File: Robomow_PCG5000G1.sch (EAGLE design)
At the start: 22 parts, among them IC1 LM339D, Q401 60N06LC, Q402 N-MOSFETDPACK, T1 2N2222, U400 74AC153D

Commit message: Commit moare reveng
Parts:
- removed IC1: LM339D, linear:LM339D
- removed R2: 2K, rcl:R-EU_R0603
- added C406, C408: (no value), rcl:C-EUC0603
- added JP1: (no value), pinhead:PINHD-2X25
- added Q403: N-MOSFETDPACK, martonmiklos:N-MOSFETDPACK
- added R210, R212, R???: 1K, resistor-dil:4R-NCAT16
- added R4, R422, R423: 2K2, rcl:R-EU_R0603
- added R???1: 2K, rcl:R-EU_R0603
- added TP703: TPB1,27, testpad:TPB1,27
- added U1: LM339M, NSC_By_element14_Batch_1.1:LM339M
- added U401: 74HC14D, 74xx-eu:74HC14D
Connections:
- removed net N$16: C407.2, R3.2
- new net MCU_P14: R210D.2
- new net MCU_P15: R210C.2
- new net MCU_P16: R210B.2
- new net MCU_P26_OUTC16_PIN45: R212B.2
- new net MCU_TA2OUT: R???B.2
- new net MOTOR_HALT?: C410.1, Q402.G, R210B.1, R406.1, R407.1
- new net MOTOR_HALT?1: C406.1, Q403.G, R210C.1
- new net N$15: U400A.1G, U401D.O
- new net N$18: C408.2, R423.1
- new net N$19: JP1.37, JP1.39, JP1.41
- new net N$20: R4.1, U1.-IN3
- new net TO_RJ11_PIN2_FROM_M16C_TXD1: JP1.4
- new net TO_RJ11_PIN_3_FROM_M16C_RXD1: JP1.3
- net GND: now also C406.2, C407.2, Q403.S, R3.2, U1.+IN4, U1.-IN4, U1.GND
- net N$12: now also R???B.1
- net N$14: now also Q403.D, R???1.2; no longer R2.2
- net N$17: now also R210D.1
- net N$5: now also C408.1, R4.2, R422.2, R423.2, U1.OUT3, U401D.I; no longer C410.1, Q402.G, R406.1, R407.1
- net N$6: now also TP703.TP
- net N$7: now also R212B.1
- net N$8: now also R???1.1, U1.+IN3; no longer IC1C.+IN, R2.1
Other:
- note added: "Motor PWM?"
- note added: "Mow PWM"
- note added: "Mow disable"
- note added: "Mow enable"
- note added: "Mow motor running if: 1G low 1C3 high A high B high"
- moved on the sheet: C407, J400, Q400, Q401, R1, R3, R407, R408, R410, R?, T1

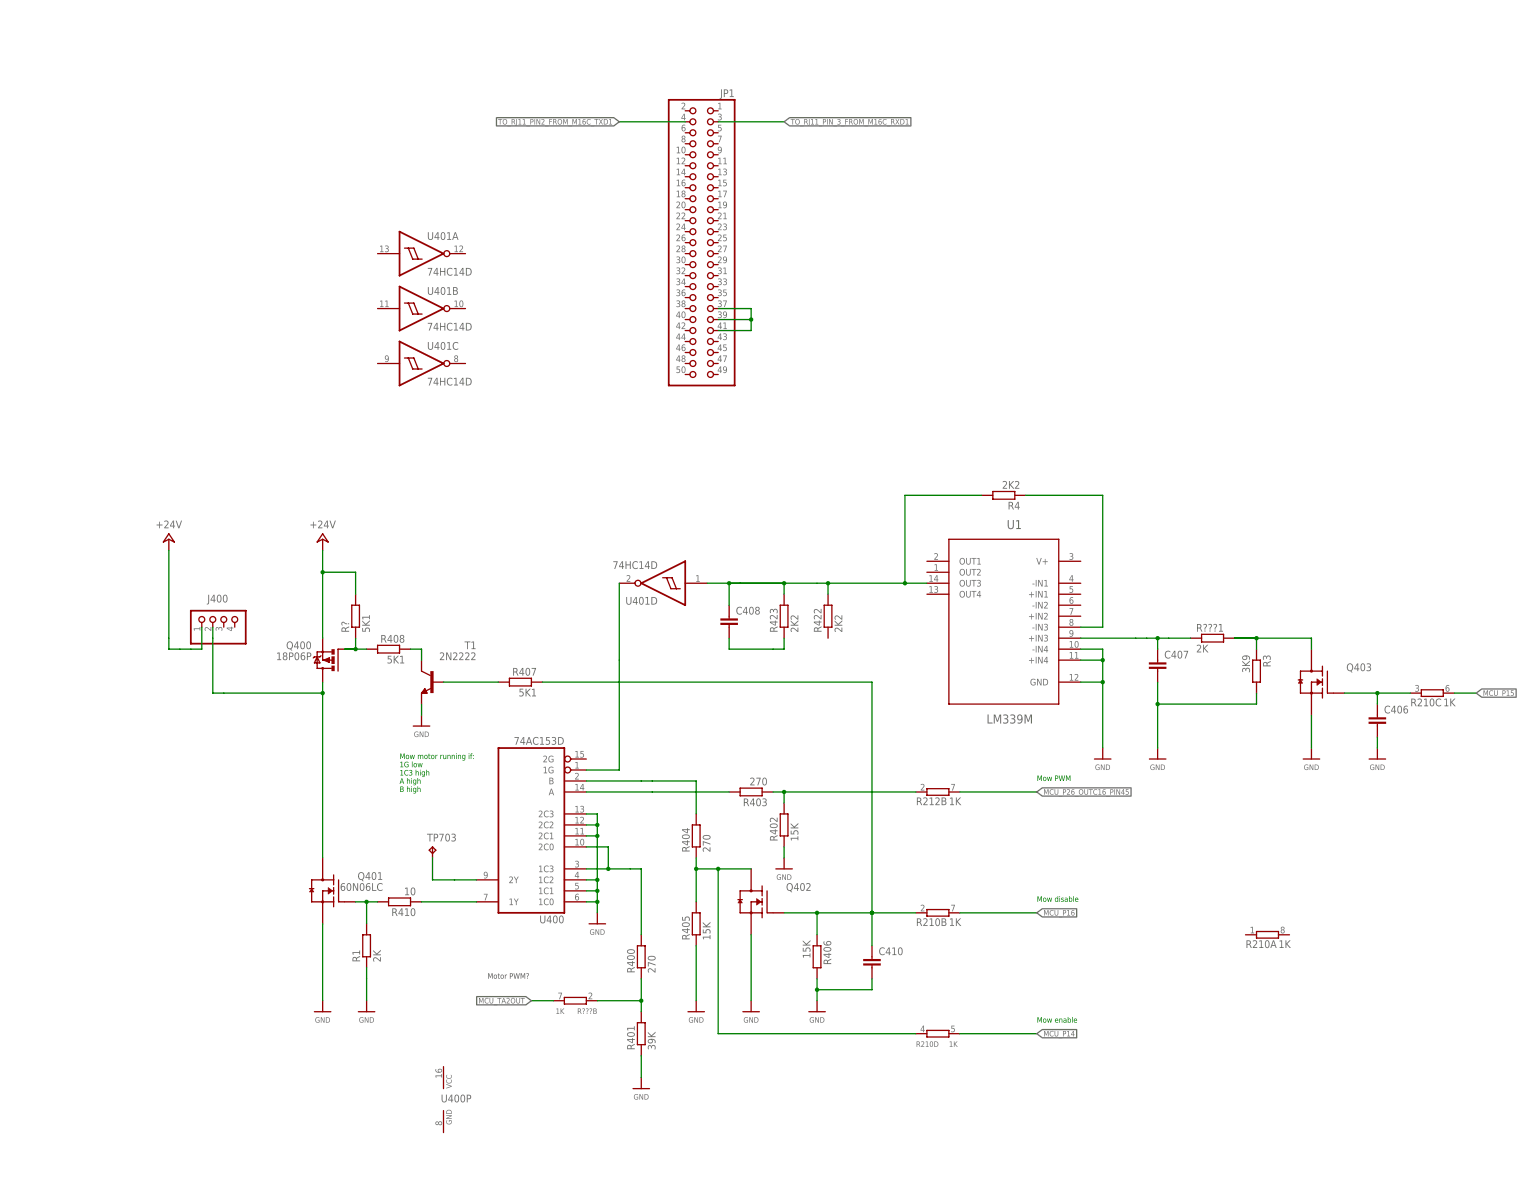
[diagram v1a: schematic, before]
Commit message: Rearranged schematic
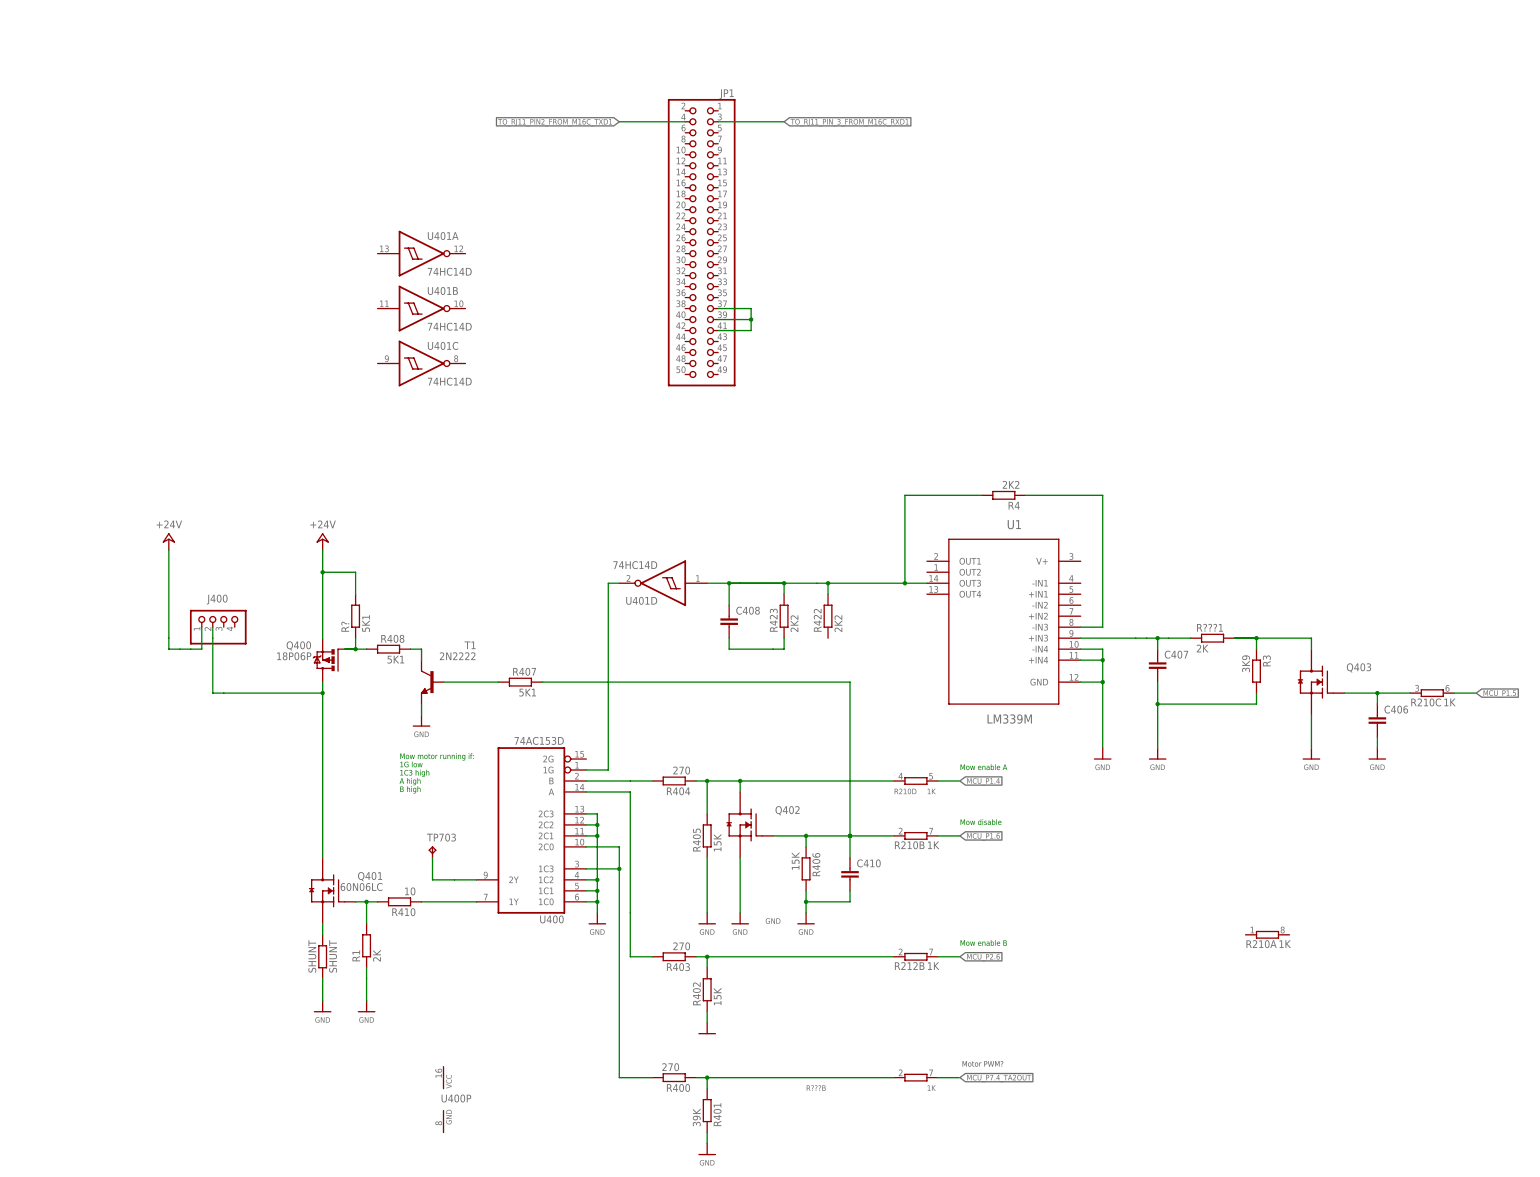
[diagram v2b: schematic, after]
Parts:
- added SHUNT: SHUNT, rcl:R-EU_R0603
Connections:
- net MCU_P14 renamed MCU_P1.4
- net MCU_P15 renamed MCU_P1.5
- net MCU_P16 renamed MCU_P1.6
- net MCU_P26_OUTC16_PIN45 renamed MCU_P2.6
- net MCU_TA2OUT renamed MCU_P7.4_TA2OUT
- new net N$16: Q401.S, SHUNT.2
- net GND: now also SHUNT.1; no longer Q401.S
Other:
- note added: "Mow enable A"
- note added: "Mow enable B"
- note removed: "Mow PWM"
- note removed: "Mow enable"
- moved on the sheet: C410, Q402, R210B, R210D, R212B, R400, R401, R402, R403, R404, R405, R406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

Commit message: Added boot trigger pin to the ribbon pinout Thanks Ryan!
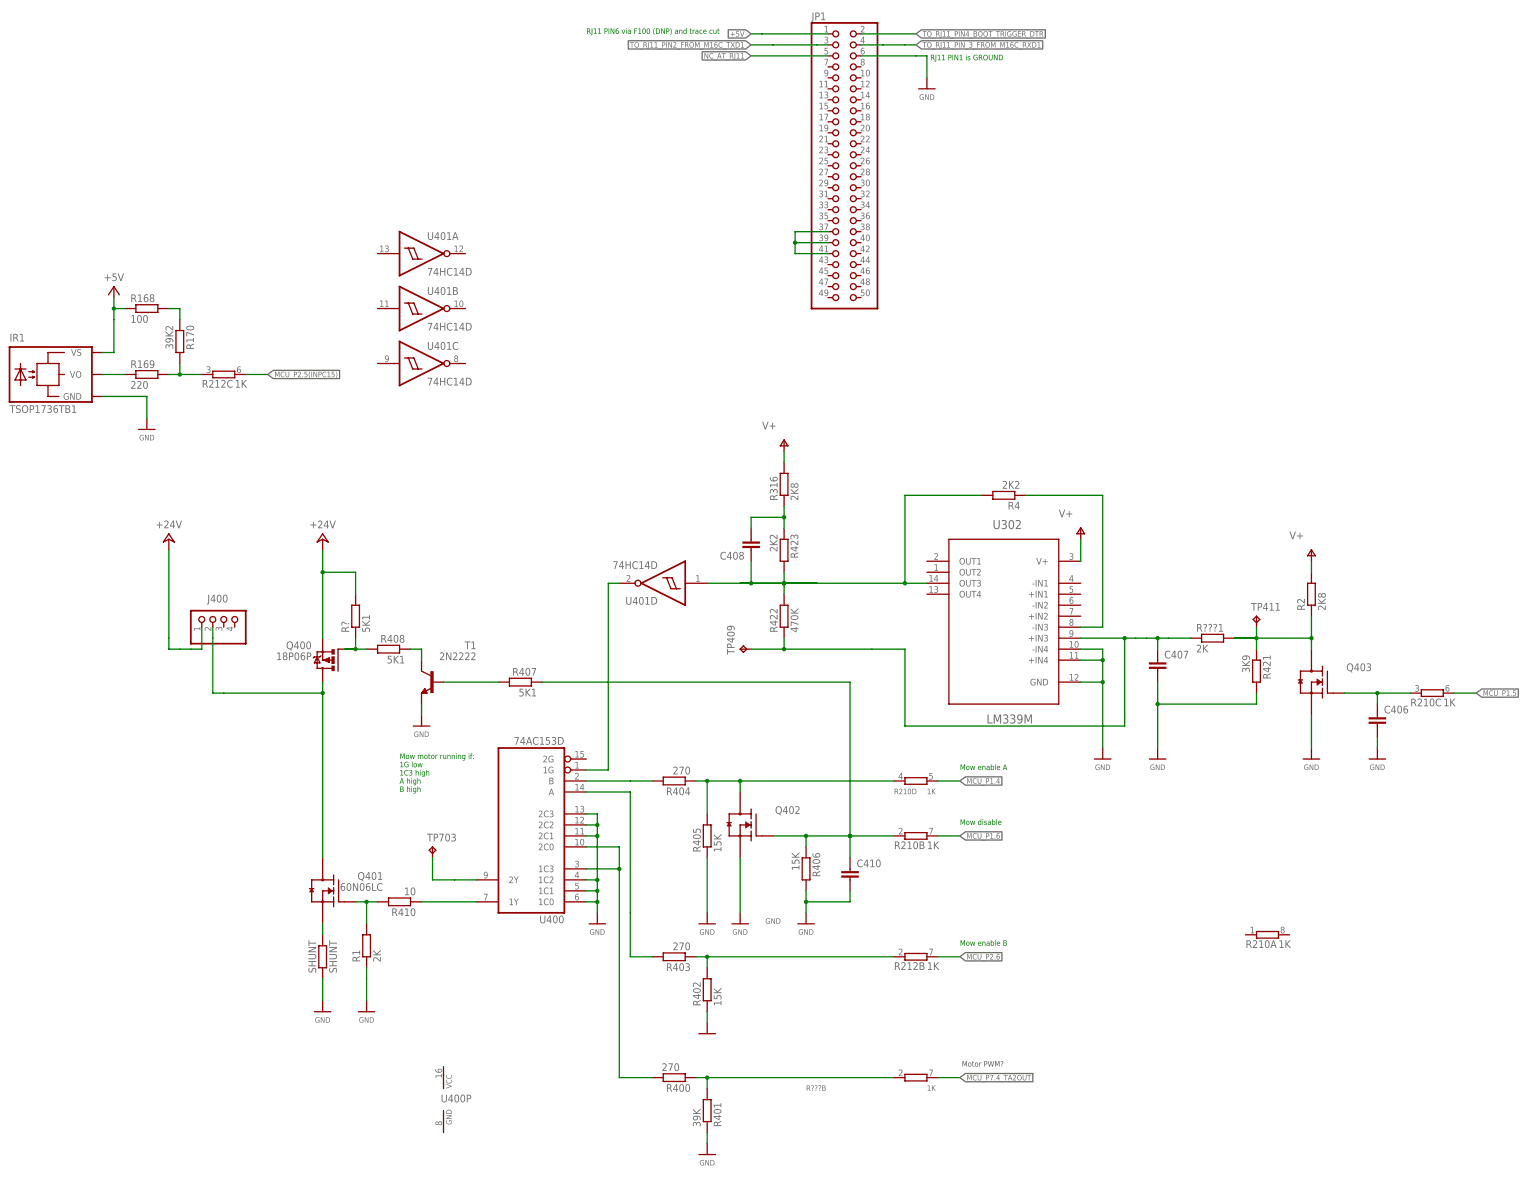
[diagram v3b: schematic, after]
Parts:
- added IR1: TSOP1736TB1, telefunken:TSOP1736TB1
- added R168: 100, rcl:R-EU_R0603
- added R169: 220, rcl:R-EU_R0603
- added R170: 39K2, rcl:R-EU_R0603
- added R2, R316: 2K8, rcl:R-EU_R0603
- added TP409, TP411: TPB1,27, testpad:TPB1,27
- R422: value 2K2 -> 470K
- renumbered R3 to R421, U1 to U302
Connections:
- new net +5V: IR1.VS, JP1.1, R168.1
- new net MCU_P2.5(INPC15): R212C.2
- new net N$21: C407.1, R422.1, R???1.1, TP409.TP, U302.+IN3
- new net N$22: IR1.VO, R169.1
- new net N$24: R168.2, R170.1
- new net NC_AT_RJ11: JP1.5
- new net TO_RJ11_PIN4_BOOT_TRIGGER_DTR: JP1.2
- new net V+: R2.2, R316.2, U302.V+
- net GND: now also IR1.GND, JP1.6
- net N$14: now also R2.1, TP411.TP
- net N$18: now also R316.1
- net N$8: now also R169.2, R170.2, R212C.1; no longer C407.1, R???1.1, U302.+IN3
- net TO_RJ11_PIN2_FROM_M16C_TXD1: now also JP1.3; no longer JP1.4
- net TO_RJ11_PIN_3_FROM_M16C_RXD1: now also JP1.4; no longer JP1.3
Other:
- note added: "RJ11 PIN1 is GROUND"
- note added: "RJ11 PIN6 via F100 (DNP) and trace cut"
- moved on the sheet: C408, JP1, R422, R423
